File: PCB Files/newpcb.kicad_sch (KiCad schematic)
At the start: 1 part, among them U1 LR2021IMLTRT

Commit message: Redid Schematic Entirely
Now have LORA tech, feather controller, many sensors, keyboard and screen. entire project revamped. need to do software next.
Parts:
- removed U1: LR2021IMLTRT, LR2021IMLTRT:QFN50P500X500X100-33N, symbol LR2021IMLTRT:LR2021IMLTRT
- added A1: Adafruit_Feather_Generic, Module:Adafruit_Feather, symbol MCU_Module:Adafruit_Feather_Generic
- added C1, C12, C14, C15, C2, C3, C5: 100nF, Capacitor_SMD:C_0603_1608Metric_Pad1.08x0.95mm_HandSolder, symbol Device:C
- added C11, C13, C4: 10nF, Capacitor_SMD:C_0603_1608Metric_Pad1.08x0.95mm_HandSolder, symbol Device:C
- added D1: LED, LED_SMD:LED_0603_1608Metric_Pad1.05x0.95mm_HandSolder, symbol Device:LED
- added J1, J2: Conn_Coaxial, Connector_Coaxial:SMA_Molex_73251-1153_EdgeMount_Horizontal, symbol Connector:Conn_Coaxial
- added J3: USB_C_Receptacle_USB2.0_16P, Connector_USB:USB_C_Receptacle_HRO_TYPE-C-31-M-12, symbol Connector:USB_C_Receptacle_USB2.0_16P
- added J4: Conn_Coaxial, Connector_Coaxial:U.FL_Molex_MCRF_73412-0110_Vertical, symbol Connector:Conn_Coaxial
- added J5: Conn_01x02(JST Vertical), Connector_JST:JST_PH_B2B-PH-K_1x02_P2.00mm_Vertical, symbol Connector_Generic:Conn_01x02
- added NT1, NT2: NetTie_2, symbol Device:NetTie_2
- added R1: 10kO, Resistor_SMD:R_0603_1608Metric_Pad0.98x0.95mm_HandSolder, symbol Device:R
- added R2, R3: 5.1kO, Resistor_SMD:R_0603_1608Metric_Pad0.98x0.95mm_HandSolder, symbol Device:R
- added R4, R5: 1kO, Resistor_SMD:R_0603_1608Metric_Pad0.98x0.95mm_HandSolder, symbol Device:R
- added R6, R7: 2.2kO, Resistor_SMD:R_0603_1608Metric_Pad0.98x0.95mm_HandSolder, symbol Device:R
- added SW1: Keyboard_6R13C, KeebDeck_Keyboard:Keyboard_6R13C, symbol KeebDeck_Keyboard:Keyboard_6R13C
- added SW2: SW_SPST(Battery Enable), Button_Switch_SMD:SW_DIP_SPSTx01_Slide_6.7x4.1mm_W6.73mm_P2.54mm_LowProfile_JPin, symbol Switch:SW_SPST
- added SW3: SW_Push(Keyboard Boot), Button_Switch_SMD:SW_Push_1TS009xxxx-xxxx-xxxx_6x6x5mm, symbol Switch:SW_Push
- added SW4: SW_Push(Feather Reset), Button_Switch_SMD:SW_Push_1TS009xxxx-xxxx-xxxx_6x6x5mm, symbol Switch:SW_Push
- added U1: Wio-LR2021, Footprint and Symbol Library:Wio-LR2021_V1, symbol Wio-LR2021_V1_sym:Wio-LR2021_V1
- added U2: MCP23017x-x-SP, Package_DIP:DIP-28_W7.62mm, symbol Interface_Expansion:MCP23017x-x-SP
- added U3: STM32F042C4Ux, Package_DFN_QFN:QFN-48-1EP_7x7mm_P0.5mm_EP5.6x5.6mm, symbol MCU_ST_STM32F0:STM32F042C4Ux
- added U4: CR2013-MI2120, Display:CR2013-MI2120, symbol Driver_Display:CR2013-MI2120
- added U5: TMP100, Package_TO_SOT_SMD:SOT-23-6, symbol Sensor_Temperature:TMP100
- added U7: 790, footprints:PA1616S_ADA, symbol 2026-07-29_00-21-30:790
- added U8: MPU-9250, Sensor_Motion:InvenSense_QFN-24_3x3mm_P0.4mm, symbol Sensor_Motion:MPU-9250
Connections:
- net GND: now also A1.4 (GND), C1.2, C11.2, C12.2, C13.1, C14.2, C15.1, C2.2, C3.2, C4.2, C5.2, J3.A1 (GND), J3.A12 (GND), J3.B1 (GND), J3.B12 (GND), J3.SH (SHIELD), J5.1 (Pin_1), NT2.2, R1.1, R2.2, R3.2, SW4.2, U2.10 (V_{SS}), U2.15 (A0), U2.16 (A1), U3.23 (VSS), U3.35 (VSS), U3.47 (VSS), U3.49 (VSS), U3.8 (VSSA), U4.2 (GND), U5.2 (GND), U8.11 (FSYNC), U8.18 (GND), U8.20 (RESV_GND), U8.9 (AD0/MISO)
- new net: A1.1 (~{RESET}), R5.2, SW4.1
- new net: J3.A5 (CC1), R3.1
- new net: R1.2, SW3.2, U3.44 (PF11)
- new net: C15.2, U8.10 (REGOUT)
- new net: A1.28 (VBAT), SW2.2 (B)
- new net: J3.A4 (VBUS), J3.A9 (VBUS), J3.B4 (VBUS), J3.B9 (VBUS)
- new net: J3.A6 (D+), J3.B6 (D+), U3.33 (PA12)
- new net: J3.A7 (D-), J3.B7 (D-), U3.32 (PA11)
- new net: J3.B5 (CC2), R2.1
- new net: D1.1 (K), R4.2
- new net: D1.2 (A), U7.5 (3D-FIX)
- new net: J5.2 (Pin_2), SW2.1 (A)
- new net: J1.1 (In), U1.10 (Sub-G_RF)
- new net: J2.1 (In), U1.13 (2.4G_RF)
- new net: J4.1 (In), U7.11 (EX_ANT)
- new net: SW1.C0, U3.18 (PB0)
- new net: SW1.C1, U3.19 (PB1)
- new net: SW1.C2, U3.20 (PB2)
- new net: SW1.C10, U3.21 (PB10)
- new net: SW1.C11, U3.22 (PB11)
- new net: SW1.C12, U3.25 (PB12)
- new net: SW1.C3, U3.39 (PB3)
- new net: SW1.C4, U3.40 (PB4)
- new net: SW1.C5, U3.41 (PB5)
- new net: SW1.C6, U3.42 (PB6)
- new net: SW1.C7, U3.43 (PB7)
- new net: SW1.C8, U3.45 (PB8)
- new net: SW1.C9, U3.46 (PB9)
- new net +3V3: A1.2 (3V3), C1.1, C11.1, C13.2, C14.1, C2.1, C3.1, C4.1, C5.1, NT1.1, R5.1, R6.1, R7.1, SW3.1, U2.17 (A2), U2.9 (V_{DD}), U3.1 (VBAT), U3.24 (VDD), U3.36 (VDDIO2), U3.48 (VDD), U3.9 (VDDA), U4.1 (VCC), U4.8 (LED), U5.3 (ADD1), U5.4 (V+), U5.5 (ADD0), U8.1 (RESV_VDDIO), U8.13 (VDD), U8.22 (~{CS}), U8.8 (VDDIO)
- new net GPS.1PPS: U2.26 (GPA5), U7.13 (1PPS)
- new net GPS.RESET: U2.25 (GPA4), U7.2 (NRESET)
- new net IMU.INT: U2.24 (GPA3), U8.12 (INT)
- new net K.INT: U2.21 (GPA0), U3.29 (PA8)
- new net K.RESET: U2.22 (GPA1), U3.7 (NRST)
- new net MISO: A1.13 (MISO), U1.4 (MISO)
- new net MOSI: A1.12 (MOSI), U1.5 (MOSI)
- new net P.INTA: A1.5 (A0), U2.20 (INTA)
- new net P.INTB: A1.6 (A1), U2.19 (INTB)
- new net P.RESET: A1.24 (D5), U2.18 (~{RESET})
- new net R.0: SW1.R0, U3.10 (PA0)
- new net R.1: SW1.R1, U3.11 (PA1)
- new net R.2: SW1.R2, U3.12 (PA2)
- new net R.3: SW1.R3, U3.13 (PA3)
- new net R.4: SW1.R4, U3.14 (PA4)
- new net R.5: SW1.R5, U3.15 (PA5)
- new net RF+3V3: C12.1, NT1.2, U1.1 (VCC_IN), U7.1 (VCC)
- new net RFGND: J1.2 (Ext), J2.2 (Ext), J4.2 (Ext), NT2.1, R4.1, U1.11 (GND), U1.12 (GND), U1.14 (GND), U1.15 (GND), U1.20 (GND), U1.9 (GND), U7.12 (GND), U7.19 (GND), U7.3 (GND), U7.8 (GND)
- new net RX: A1.14 (RX), U7.10 (RX0)
- new net SC.CLK: A1.10 (A5), U4.7 (SCK)
- new net SC.CS: A1.7 (A2), U4.3 (~{CS})
- new net SC.D/C: A1.25 (D6), U4.5 (D/~{C})
- new net SC.MISO: A1.8 (A3), U4.9 (MISO)
- new net SC.MOSI: A1.9 (A4), U4.6 (MOSI)
- new net SC.RESET: U2.23 (GPA2), U4.4 (RESET)
- new net SCK: A1.11 (SCK), U1.6 (SCK)
- new net SCL: A1.18 (SCL), R6.2, U2.12 (SCK), U3.30 (PA9), U5.1 (SCL), U8.23 (SCL/SCLK)
- new net SDA: A1.17 (SDA), R7.2, U2.13 (SDA), U3.31 (PA10), U5.6 (SDA), U8.24 (SDA/MOSI)
- new net T.BAND: A1.20 (D1), U1.21 (DIO6)
- new net T.BUSY: A1.22 (D3), U1.8 (BUSY)
- new net T.CS: A1.21 (D2), U1.7 (NSS)
- new net T.INT: A1.19 (D0), U1.22 (DIO7)
- new net T.RESET: A1.23 (D4), U1.3 (RESET)
- new net TX: A1.15 (TX), U7.9 (TX0)
- no-connect marks 0 -> 45

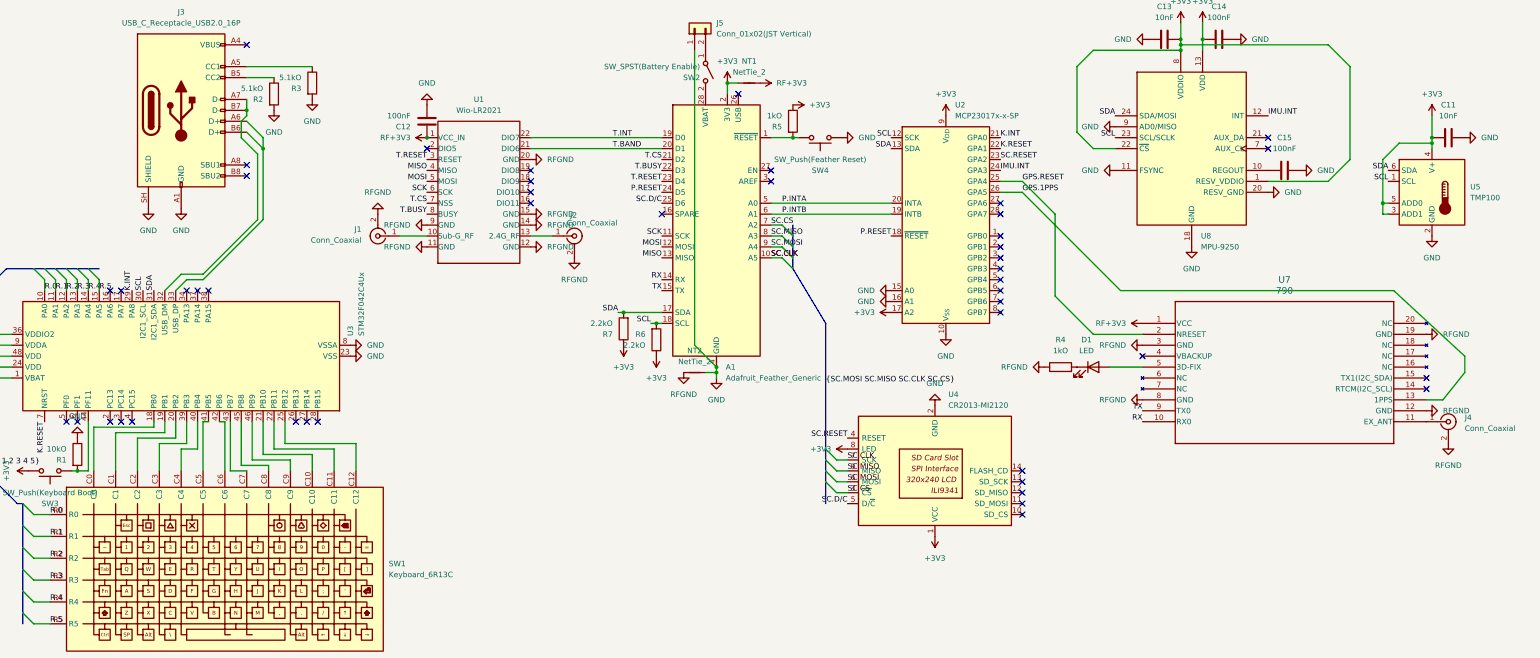
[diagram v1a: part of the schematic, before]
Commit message: Updated PCB, worked on radio section, positioned chips and stuff on board
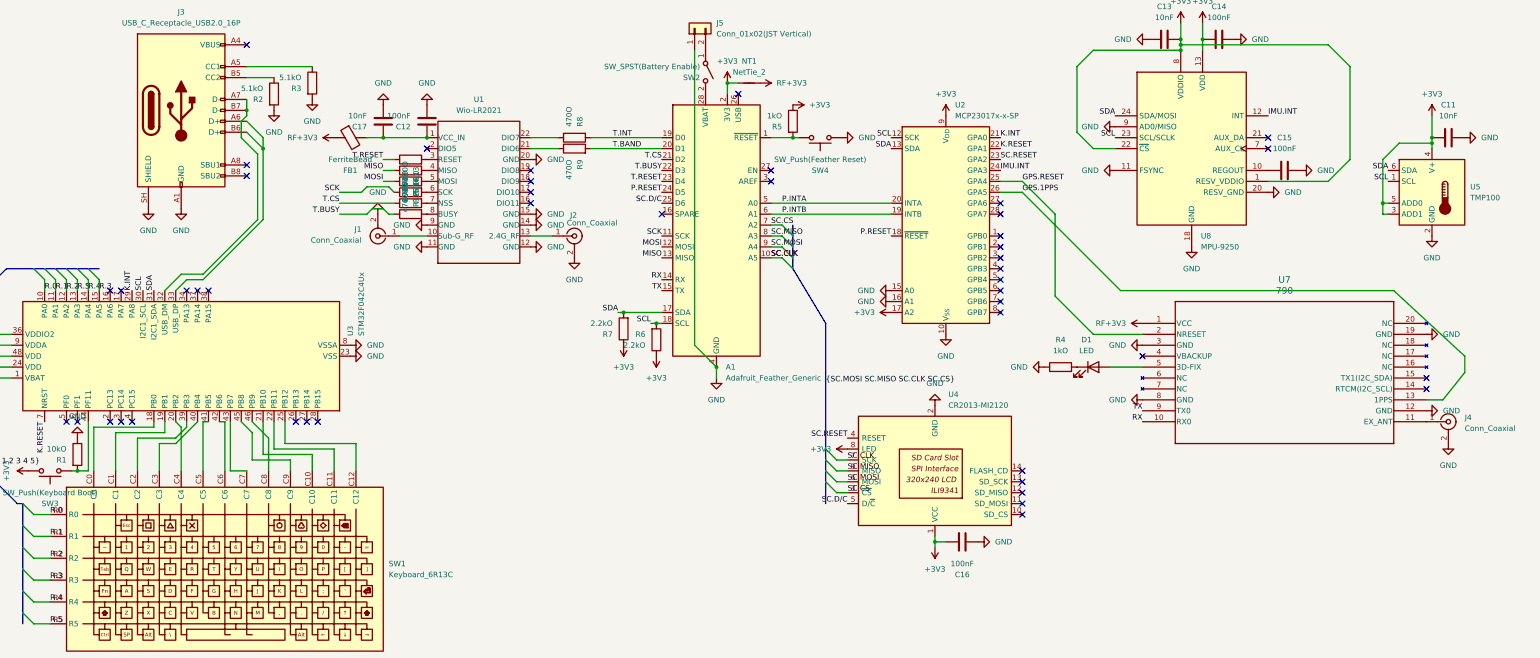
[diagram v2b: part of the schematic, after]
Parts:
- removed NT2: NetTie_2, symbol Device:NetTie_2
- added C16: 100nF, Capacitor_SMD:C_0603_1608Metric_Pad1.08x0.95mm_HandSolder, symbol Device:C
- added C17: 10nF, Capacitor_SMD:C_0603_1608Metric_Pad1.08x0.95mm_HandSolder, symbol Device:C
- added FB1: FerriteBead, Inductor_SMD:L_0603_1608Metric_Pad1.05x0.95mm_HandSolder, symbol Device:FerriteBead
- added R10, R11, R12, R13, R14, R15, R8, R9: 470O, Resistor_SMD:R_0603_1608Metric_Pad0.98x0.95mm_HandSolder, symbol Device:R
- NT1: footprint (none) -> NetTie:NetTie-2_SMD_Pad2.0mm
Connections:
- net RFGND is gone; now on net GND: J1.2 (Ext), J2.2 (Ext), J4.2 (Ext), R4.1, U1.11 (GND), U1.12 (GND), U1.14 (GND), U1.15 (GND), U1.20 (GND), U1.9 (GND), U7.12 (GND), U7.19 (GND), U7.3 (GND), U7.8 (GND)
- net +3V3: now also C16.1
- net GND: now also C16.2, C17.2
- net MISO: now also R11.1; no longer U1.4 (MISO)
- net MOSI: now also R12.1; no longer U1.5 (MOSI)
- net R.3: now also U3.15 (PA5); no longer U3.13 (PA3)
- net R.5: now also U3.13 (PA3); no longer U3.15 (PA5)
- net RF+3V3: now also FB1.1; no longer C12.1, U1.1 (VCC_IN)
- net SCK: now also R13.1; no longer U1.6 (SCK)
- net T.BAND: now also R9.2; no longer U1.21 (DIO6)
- net T.BUSY: now also R15.1; no longer U1.8 (BUSY)
- net T.CS: now also R14.1; no longer U1.7 (NSS)
- net T.INT: now also R8.2; no longer U1.22 (DIO7)
- net T.RESET: now also R10.1; no longer U1.3 (RESET)
- net at U3.20 (PB2): now also SW1.C4; no longer SW1.C2
- net at U3.39 (PB3): now also SW1.C2; no longer SW1.C3
- net at U3.40 (PB4): now also SW1.C3; no longer SW1.C4
- net at U3.45 (PB8): now also SW1.C9; no longer SW1.C8
- net at U3.46 (PB9): now also SW1.C8; no longer SW1.C9
- new net: R14.2, U1.7 (NSS)
- new net: C12.1, C17.1, FB1.2, U1.1 (VCC_IN)
- new net: R10.2, U1.3 (RESET)
- new net: R8.1, U1.22 (DIO7)
- new net: R13.2, U1.6 (SCK)
- new net: R11.2, U1.4 (MISO)
- new net: R15.2, U1.8 (BUSY)
- new net: R9.1, U1.21 (DIO6)
- new net: R12.2, U1.5 (MOSI)

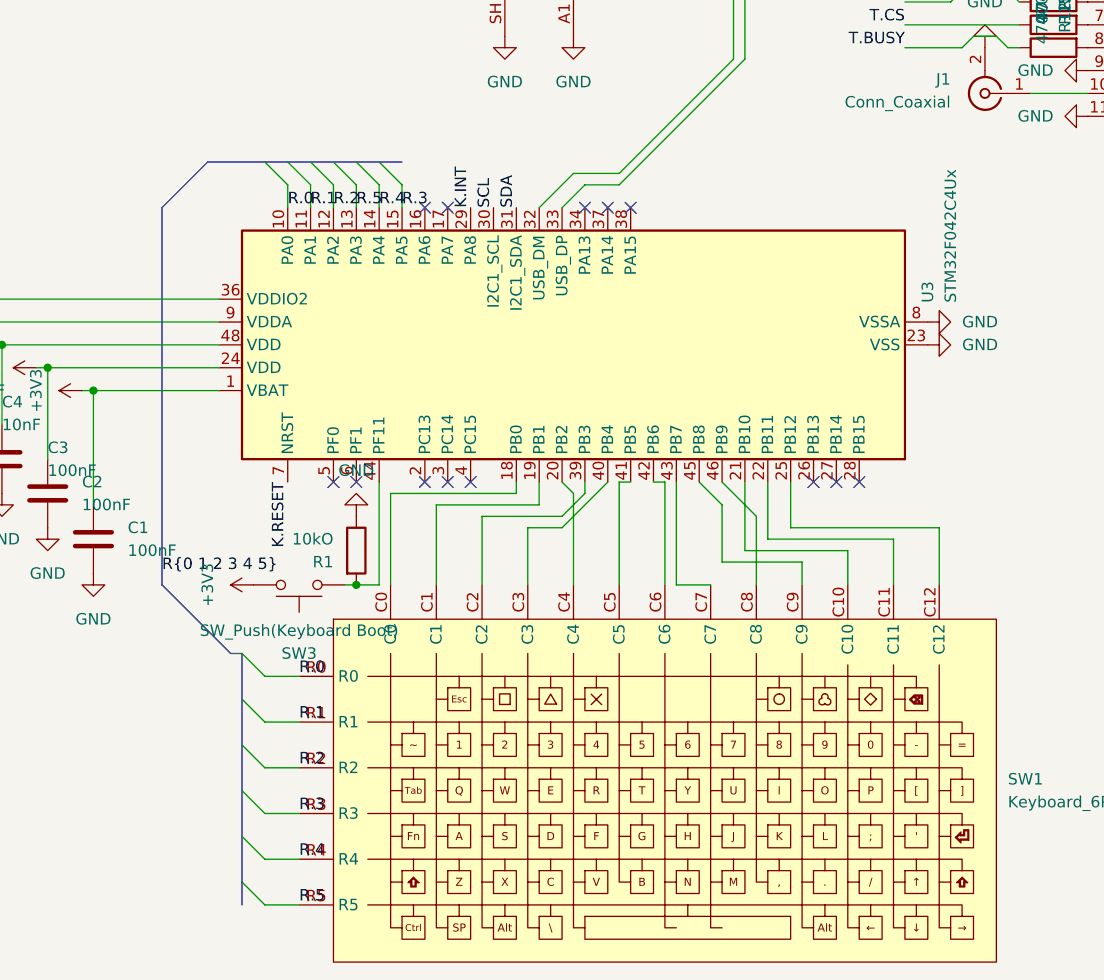
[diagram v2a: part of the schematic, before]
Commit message: Finished keyboard controller matrix, did some wiring
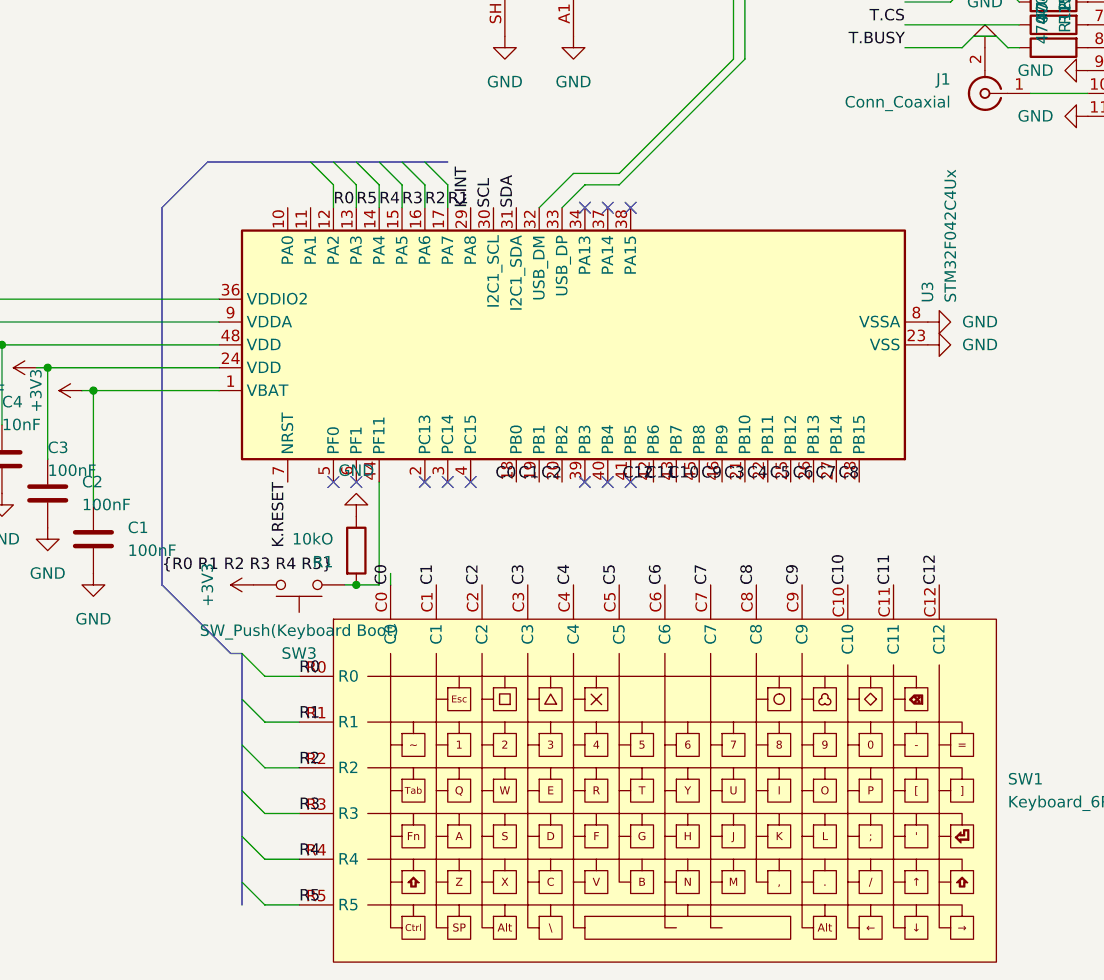
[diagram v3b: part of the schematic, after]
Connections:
- net R2: now reaches U3.16 (PA6)
- net R2: now also SW1.R2
- net R1: now reaches U3.17 (PA7)
- net R1: now also SW1.R1
- net C0: now reaches SW1.C0, U3.18 (PB0)
- net C1: now reaches SW1.C1, U3.19 (PB1)
- net C2: now reaches U3.20 (PB2)
- net C2: now also SW1.C2; no longer SW1.C4
- net C10: now reaches SW1.C10
- net C10: now also U3.45 (PB8); no longer U3.21 (PB10)
- net C11: now reaches SW1.C11
- net C11: now also U3.43 (PB7); no longer U3.22 (PB11)
- net C12: now reaches SW1.C12
- net C12: now also U3.42 (PB6); no longer U3.25 (PB12)
- net C6: now reaches U3.26 (PB13)
- net C6: now also SW1.C6
- net C7: now reaches U3.27 (PB14)
- net C7: now also SW1.C7
- net C8: now reaches U3.28 (PB15)
- net C8: now also SW1.C8
- net at U3.39 (PB3): no longer SW1.C2
- net at U3.40 (PB4): no longer SW1.C3
- net at U3.41 (PB5): no longer SW1.C5
- net C9: now reaches SW1.C9
- net C9: now also U3.46 (PB9); no longer U3.45 (PB8)
- net R.0: no longer names the net of U3.10 (PA0)
- net R.0: no longer SW1.R0
- net R.1: no longer names the net of U3.11 (PA1)
- net R.1: no longer SW1.R1
- net R.2 renamed R0
- net R0: now also SW1.R0; no longer SW1.R2
- net R.3 renamed R3
- net R.4 renamed R4
- net R.5 renamed R5
- new net C3: SW1.C3, U3.21 (PB10)
- new net C4: SW1.C4, U3.22 (PB11)
- new net C5: SW1.C5, U3.25 (PB12)
- no-connect marks 45 -> 43

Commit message: Finish PCB, yay
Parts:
- removed C13: 10nF, Capacitor_SMD:C_0603_1608Metric_Pad1.08x0.95mm_HandSolder, symbol Device:C
- removed C14, C15: 100nF, Capacitor_SMD:C_0603_1608Metric_Pad1.08x0.95mm_HandSolder, symbol Device:C
- removed U8: MPU-9250, Sensor_Motion:InvenSense_QFN-24_3x3mm_P0.4mm, symbol Sensor_Motion:MPU-9250
- added C6: 220nF, Capacitor_SMD:C_0603_1608Metric_Pad1.08x0.95mm_HandSolder, symbol Device:C
- added C7, C9: 100nF, Capacitor_SMD:C_0603_1608Metric_Pad1.08x0.95mm_HandSolder, symbol Device:C
- added C8: 10nF, Capacitor_SMD:C_0603_1608Metric_Pad1.08x0.95mm_HandSolder, symbol Device:C
- added U6: LSM303AGR, LSM303AGR:PQFN50P200X200X100-12N, symbol LSM303AGR:LSM303AGR
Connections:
- net +3V3: now also C7.1, C8.1, C9.1, U6.10 (VDD_IO), U6.2 (CS_XL), U6.3 (CS_MAG), U6.9 (VDD)
- net GND: now also C6.1, C7.2, C8.2, C9.2, U6.6 (GND), U6.8 (GND)
- net SCL: now also U6.1 (SCL/SPC)
- net SDA: now also U6.4 (SDA/SDI/SDO)
- net INT_2_XL: now reaches U2.27 (GPA6)
- net INT_2_XL: now also U6.11 (INT_2_XL)
- net INT_MAG/DRDY: now reaches U2.28 (GPA7)
- net INT_MAG/DRDY: now also U6.7 (INT_MAG/DRDY)
- net GPS.1PPS: no longer names the net of U7.13 (1PPS)
- net GPS.1PPS: no longer U2.26 (GPA5)
- new net: C6.2, U6.5 (C1)
- new net INT_1_XL: U2.26 (GPA5), U6.12 (INT_1_XL)
- no-connect marks 43 -> 42
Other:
- moved on the sheet: C11, U5

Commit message: fix error in gps uart
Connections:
- net RX: now also U7.9 (TX0); no longer U7.10 (RX0)
- net TX: now also U7.10 (RX0); no longer U7.9 (TX0)
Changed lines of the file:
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@@
 	)
 	(label "RX"
-		(at 318.77 163.83 180)
+		(at 318.77 161.29 180)
 		(effects
 			(font
@@
 	)
 	(label "TX"
-		(at 318.77 161.29 180)
+		(at 318.77 163.83 180)
 		(effects
 			(font
